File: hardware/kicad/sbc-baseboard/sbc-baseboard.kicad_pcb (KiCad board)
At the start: 6 copper layers, 140 x 100 mm, 271 parts, among them J1 USB-C upstream, J10 RJ45 magjack 10/100, J11 COM/NO/NC, J12 COM/NO/NC, J13 Console, J14 +5V_TGT out, J15 GPIO + I2C, J16 SWD, J18 PSU in (isolated), J19 PSU out (isolated), J2 5 V in, 2.5 mm, J3 USB-C HID to target, J4 USB-A x2, J5 USB-A x2, J601 SWD (K20), J9 FTDI header, K801 G6K-2F-Y DC5, K802 G6K-2F-Y DC5, K803 JW1FSN-DC5V, Q101 DMP3013SFV, Q801 2N7002, Q802 2N7002, Q803 AO3400A, SW201 RESET, SW601 DAP RESET, U105 TPS62823DLC, U201 MK64FN1M0VLL12, U202 USBLC6-2SC6, U301 KSZ8081RNA, U401 USBLC6-2SC6, U402 USB2517, U403 TPS2553DBV, U404 TPS2553DBV, U405 TPS2553DBV, U406 TPS2553DBV, U407 TPS2553DBV, U408 USBLC6-2SC6, U409 USBLC6-2SC6, U410 USBLC6-2SC6, U411 USBLC6-2SC6, U501 FT231XS, U601 MK20DX128VFM5, U701 TXB0104PW, U702 TXB0108PW, U703 TXS0102DCU, U704 TPS26630RGE, U801 LTV-817, Y201 32.768kHz, Y301 25MHz, Y401 24MHz, Y601 8MHz

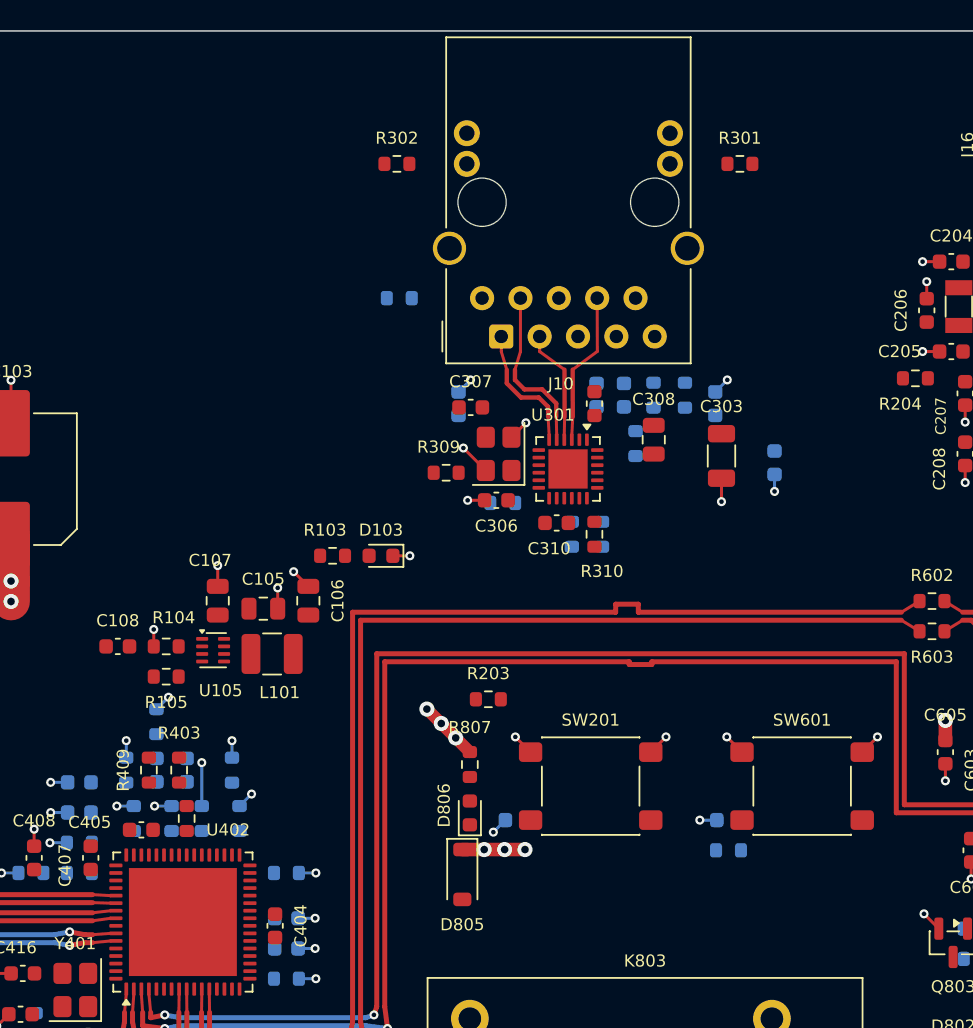
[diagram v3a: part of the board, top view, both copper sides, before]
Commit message: The RJ45 another 10 mm left, the two reset buttons in a column beside it on the back edge
J10 from x 55 to x 45, the PHY and the magnetics void with it; SW201 and
SW601 from the centre band to (71.5, 8) and (71.5, 17), one above the
other on the jack's right with 2 mm of void between them and from the
jack, inside the edge zone. The centre band is free again. Placed and
gated, unrouted.

Co-Authored-By: Claude Fable 5.1 <noreply@anthropic.com>
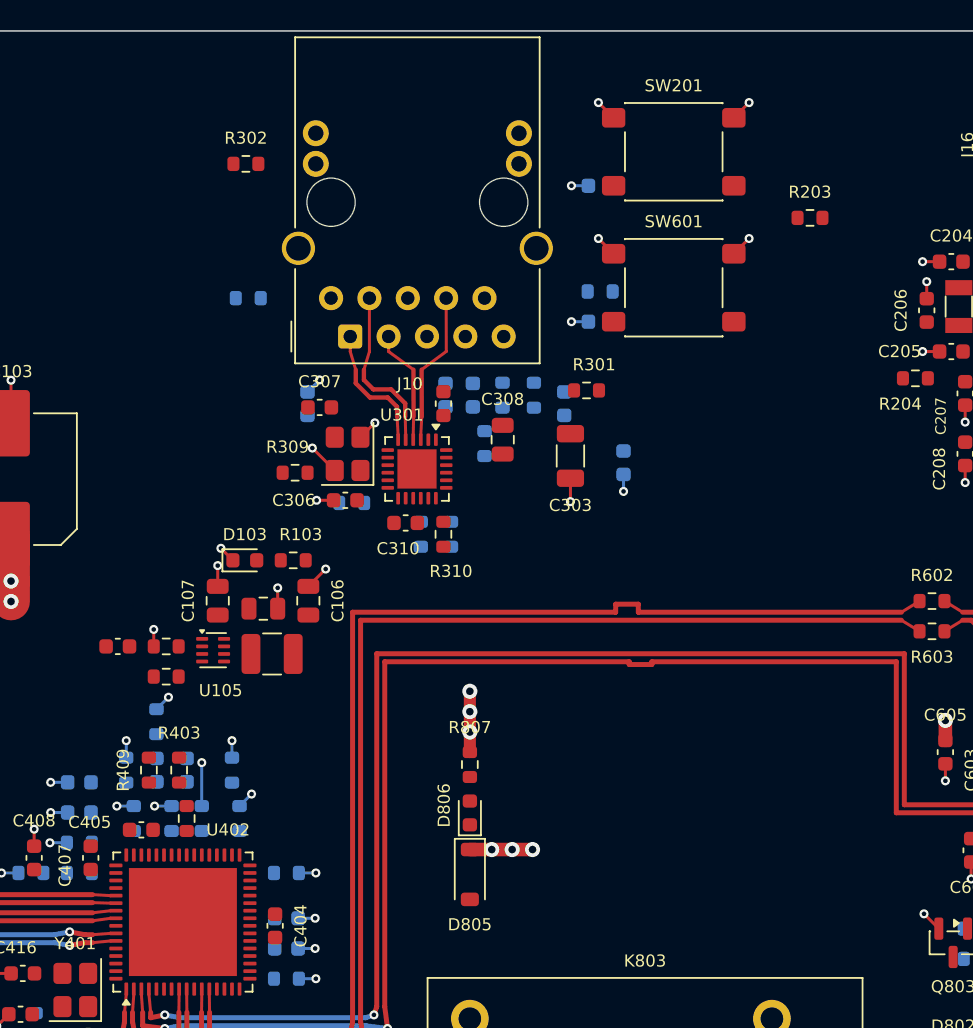
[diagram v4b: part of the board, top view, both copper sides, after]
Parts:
- moved C203 42.4 mm to (66.6, 10.2)
- moved SW201 42.4 mm to (71.5, 8.00)
- moved R203 38.3 mm to (80.5, 12.4), turned to 180 degrees
- moved R604 38.0 mm to (66.6, 17.2)
- moved C601 34.1 mm to (66.6, 19.2)
- moved SW601 34.1 mm to (71.5, 17.0)
- moved R301 18.1 mm to (65.7, 23.8)
- moved C301 10.0 mm to (56.4, 24.1)
- moved C302 10.0 mm to (58.2, 24.1)
- moved C303 10.0 mm to (64.7, 28.1)
- moved C304 10.0 mm to (64.2, 24.7)
- moved C305 10.0 mm to (47.2, 24.7)
- moved C306 10.0 mm to (49.8, 31.1)
- moved C307 10.0 mm to (48.1, 24.9)
- moved C308 10.0 mm to (60.2, 27.1)
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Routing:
- net GND: track 154.6 -> 153.7 mm, vias 118 -> 117

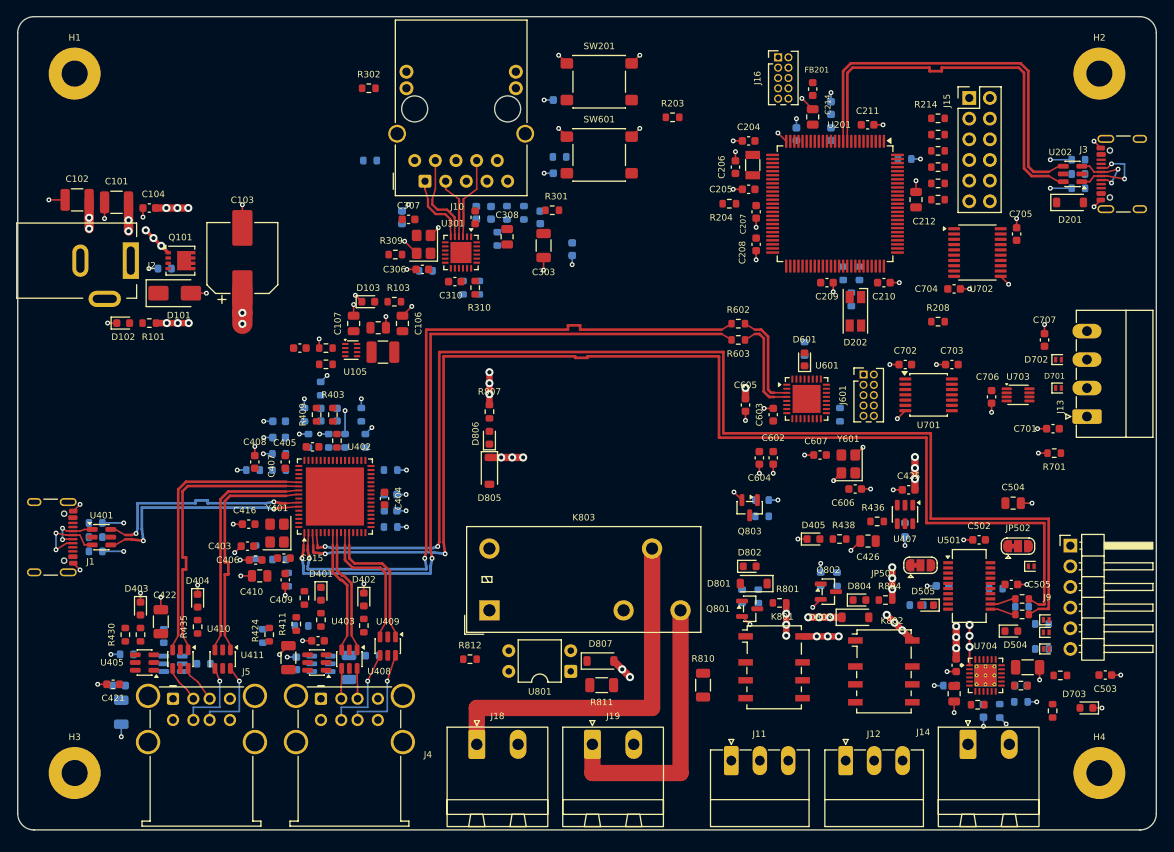
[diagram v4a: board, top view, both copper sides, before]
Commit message: The owner's first hand-placement pass over the barrel-inlet board: 133 of 271 parts moved
Placed in KiCad over the generated placement of 99e18b0: the upstream
USB-C to y 52 with its array, the inlet 5 mm up with its parts regrouped,
the 3V3 buck and its island to the inlet's side, the K64 7 mm left with
its decoupling re-laid, the DAPLink and its SWD header 15 mm left into
the centre, the shifters and the FTDI switch regrouped, the port
switches' pull-ups moved from the K64 to the switches, three parts to
the bottom. Unrouted. The generator is retooled next to reproduce it.

Co-Authored-By: Claude Fable 5.1 <noreply@anthropic.com>
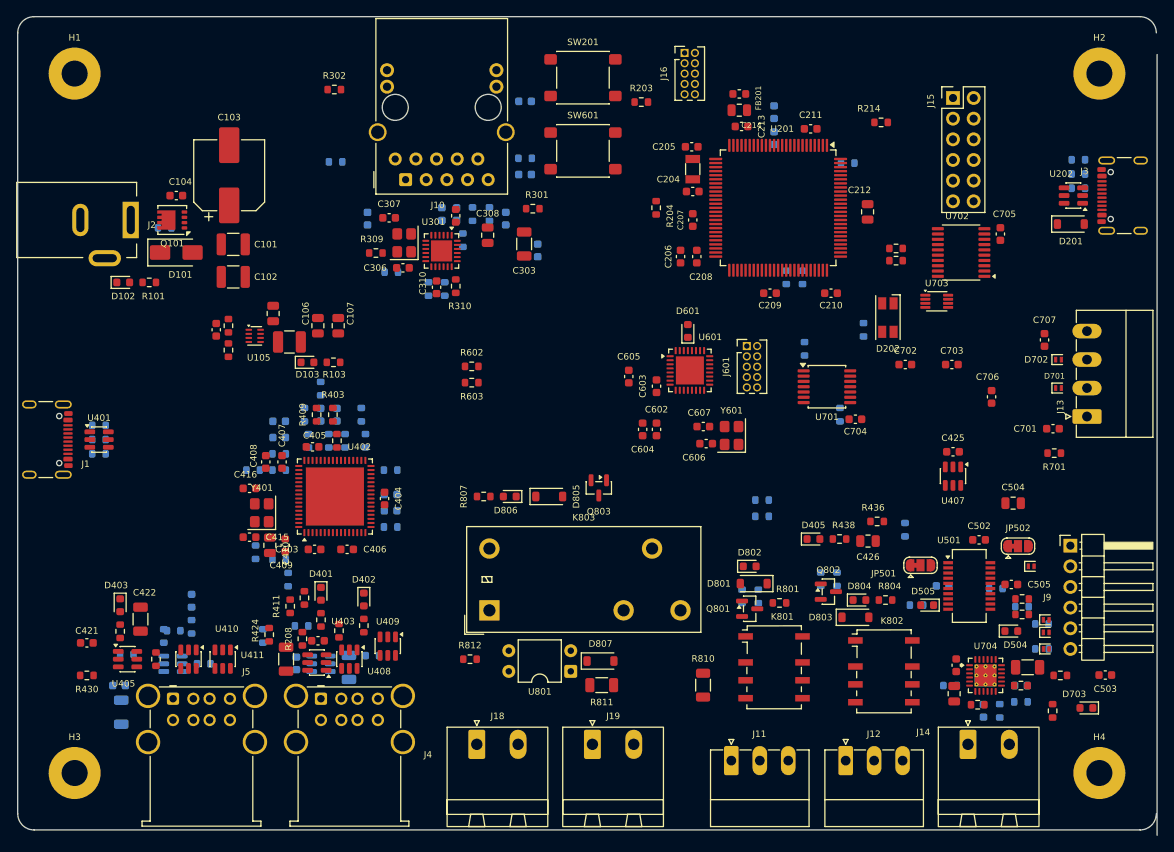
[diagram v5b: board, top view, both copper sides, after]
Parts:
- C213: moved to F.Cu
- D404, R211, R435: moved to B.Cu
- moved R210 114.7 mm to (17.0, 79.0), turned to 90 degrees
- moved R211 112.0 mm to (19.2, 75.5), turned to 180 degrees
- moved R209 93.1 mm to (39.5, 75.5), turned to 90 degrees
- moved R208 87.3 mm to (35.0, 76.5), turned to 90 degrees
- moved R602 33.2 mm to (55.8, 43.0)
- moved R603 33.2 mm to (55.8, 45.0)
- moved C102 21.4 mm to (26.5, 32.0), turned to 0 degrees
- moved C704 20.1 mm to (103.0, 49.5)
- moved C606 19.2 mm to (84.7, 52.5)
- moved Q803 18.7 mm to (71.5, 57.9)
- moved C101 15.3 mm to (26.5, 28.0), turned to 0 degrees
- moved U703 15.2 mm to (113.0, 35.0)
- moved C602 14.8 mm to (78.5, 50.8)
- moved C603 14.8 mm to (78.5, 45.4)
- moved C604 14.8 mm to (76.8, 50.8)
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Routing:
- net GND: track 153.7 -> 0.00 mm, vias 117 -> 0
- net HUB_DN2_N: track 149.5 -> 0.00 mm, vias 2 -> 0
- net HUB_DN2_P: track 149.5 -> 0.00 mm, vias 2 -> 0
- net HUB_DN1_P: track 87.1 -> 0.00 mm, vias 2 -> 0
- net HUB_DN1_N: track 87.1 -> 0.00 mm, vias 2 -> 0
- net +5V: track 67.1 -> 0.00 mm, vias 46 -> 0
- net /MCU/K64_USB_N: track 47.4 -> 0.00 mm
- net /MCU/K64_USB_P: track 47.4 -> 0.00 mm
- net /Relays/PSU_VP: track 45.6 -> 0.00 mm
- net /Relays/PSU_VOUT: track 34.4 -> 0.00 mm
- net /USB hub/HUB_DN6_N: track 34.2 -> 0.00 mm
- net /USB hub/HUB_DN6_P: track 34.2 -> 0.00 mm
- net /USB hub/HUB_DN7_N: track 27.8 -> 0.00 mm
- net /USB hub/HUB_DN7_P: track 27.8 -> 0.00 mm
- net /USB hub/HUB_UP_N: track 26.7 -> 0.00 mm, vias 2 -> 0
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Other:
- board size 140 x 100 mm -> 140.1 x 100.7 mm

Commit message: The generator reproduces the owner's hand placement: every part's pose harvested into gen/hand_placement.py
The standard's tools/handplace.py (ecad-standards ca75146..fe3) reads every
footprint's pose off the hand-placed board (c1628c5) into
gen/hand_placement.py as HAND, 254 parts (84 on the bottom); layout.py
merges HAND over FIXED, so a hand-fixed part outranks its anchor and the
engine's own rule, and the edge connectors J1, J2, J3 and J10 have the
positions the hand pass gave them in CONNECTORS. The regenerated board is
the hand-placed one, part for part (handplace.py --check: 0 placed
elsewhere, 0 missing; 271 fixed).

placement.txt ends with the engine's new "hand placement" section: 24
hand-fixed parts closer than the packing margin to a neighbour, the lanes
that run through hand-placed parts (C403 and C406 under the hub's
downstream pins, Y401 and C416 at its upstream pins, R209 under U408, C605,
C603 and J601 at the DAPLink, C606, Y601 and C607 on HUB_DN2's old path,
C301 under the ETH lanes, R211, R435 and D404 under HUB_DN6 on the bottom),
and K20_USB laid with its members crossing because its path enters the
turned DAPLink from the wrong side. The DRC gate reports 138 errors, all
from those lanes and six hand-placed courtyard overlaps; the lanes are
redrawn once the hand placement settles, and the board is not routed before
the gate is clean. Documented in docs/layout-directives.md (the hand loop,
the anchors table's standing) and hardware/kicad/README.md (the state);
KiCad lock files ignored.

Co-Authored-By: Claude Fable 5.1 <noreply@anthropic.com>
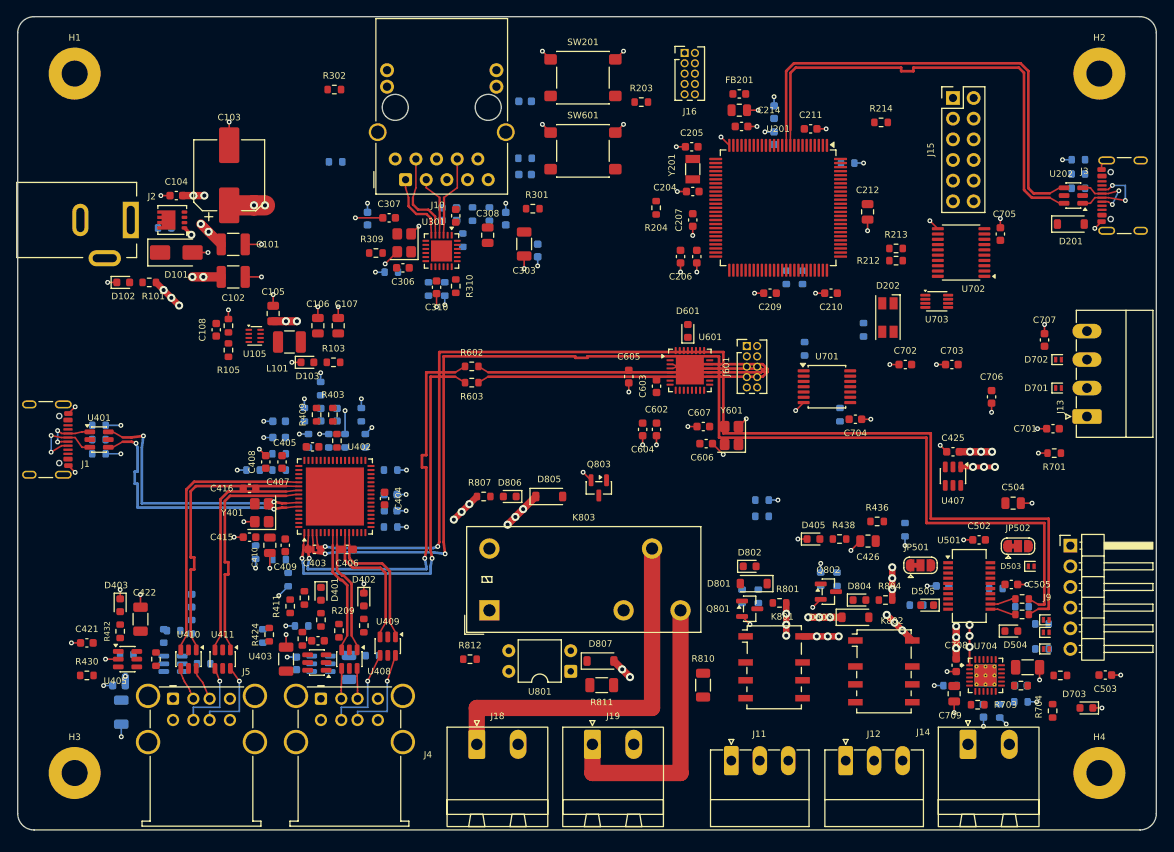
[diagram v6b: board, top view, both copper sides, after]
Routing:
- net GND: track 0.00 -> 151.1 mm, vias 0 -> 115
- net HUB_DN2_N: track 0.00 -> 149.5 mm, vias 0 -> 2
- net HUB_DN2_P: track 0.00 -> 149.5 mm, vias 0 -> 2
- net +5V: track 0.00 -> 70.7 mm, vias 0 -> 48
- net /MCU/K64_USB_N: track 0.00 -> 57.7 mm
- net /MCU/K64_USB_P: track 0.00 -> 57.7 mm
- net HUB_DN1_P: track 0.00 -> 49.0 mm, vias 0 -> 2
- net HUB_DN1_N: track 0.00 -> 49.0 mm, vias 0 -> 2
- net /DAPLink/K20_USB_N: track 0.00 -> 48.3 mm
- net /DAPLink/K20_USB_P: track 0.00 -> 47.5 mm
- net /Relays/PSU_VP: track 0.00 -> 45.6 mm
- net /Relays/PSU_VOUT: track 0.00 -> 34.4 mm
- net /USB hub/HUB_DN6_N: track 0.00 -> 33.2 mm
- net /USB hub/HUB_DN6_P: track 0.00 -> 33.2 mm
- net /USB hub/HUB_UP_P: track 0.00 -> 31.2 mm, vias 0 -> 2
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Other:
- board size 140.1 x 100.7 mm -> 140 x 100 mm
